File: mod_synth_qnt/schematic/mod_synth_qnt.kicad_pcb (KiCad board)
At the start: 2 copper layers, 41.3 x 109.2 mm, 37 parts, among them J1 CV IN, J2 Conn_02x08_Odd_Even, J3 QUANTIZE OUT, J4 Conn_01x07_Male, J5 Conn_01x07_Female, J6 Conn_01x07_Female, J7 Conn_01x07_Male, U1 LM358

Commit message: finish layout
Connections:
- A1 pad 5: /LED_A -> Net-(A1-Pad5)
- A1 pad 6: /LED_B -> Net-(A1-Pad6)
- A1 pad 7: /LED_C -> Net-(A1-Pad7)
- A1 pad 8: /LED_D -> Net-(A1-Pad8)
- C4 pad 1: /SCALE_SELECT -> /SCALE_SELECT_PCB_B
- C5 pad 1: /NOTE_SELECT -> /NOTE_SELECT_PCB_B
- D10 pad 1: Net-(D10-Pad1) -> /LED_B_PCB_B
- D10 pad 2: Net-(D10-Pad2) -> /LED_D_PCB_B
- D11 pad 1: Net-(D10-Pad2) -> /LED_D_PCB_B
- D11 pad 2: Net-(D10-Pad1) -> /LED_B_PCB_B
- D12 pad 1: Net-(D12-Pad1) -> /LED_A_PCB_B
- D12 pad 2: Net-(D10-Pad2) -> /LED_D_PCB_B
- D13 pad 1: Net-(D10-Pad2) -> /LED_D_PCB_B
- D13 pad 2: Net-(D12-Pad1) -> /LED_A_PCB_B
- D2 pad 1: Net-(D12-Pad1) -> /LED_A_PCB_B
- D2 pad 2: Net-(D10-Pad1) -> /LED_B_PCB_B
- D3 pad 1: Net-(D10-Pad1) -> /LED_B_PCB_B
- D3 pad 2: Net-(D3-Pad2) -> /LED_C_PCB_B
- D4 pad 1: Net-(D3-Pad2) -> /LED_C_PCB_B
- D4 pad 2: Net-(D10-Pad2) -> /LED_D_PCB_B
- D5 pad 1: Net-(D10-Pad1) -> /LED_B_PCB_B
- D5 pad 2: Net-(D12-Pad1) -> /LED_A_PCB_B
- D6 pad 1: Net-(D3-Pad2) -> /LED_C_PCB_B
- D6 pad 2: Net-(D10-Pad1) -> /LED_B_PCB_B
- D7 pad 1: Net-(D10-Pad2) -> /LED_D_PCB_B
- D7 pad 2: Net-(D3-Pad2) -> /LED_C_PCB_B
- D8 pad 1: Net-(D12-Pad1) -> /LED_A_PCB_B
- D8 pad 2: Net-(D3-Pad2) -> /LED_C_PCB_B
- D9 pad 1: Net-(D3-Pad2) -> /LED_C_PCB_B
- D9 pad 2: Net-(D12-Pad1) -> /LED_A_PCB_B
- J4 pad 5: Net-(J4-Pad5) -> /5V_PCB_B
- J5 pad 5: Net-(J5-Pad5) -> +5V
- J6 pad 2: Net-(J6-Pad2) -> /LED_A
- J6 pad 3: Net-(J6-Pad3) -> /LED_B
- J6 pad 4: Net-(J6-Pad4) -> /LED_C
- J6 pad 5: Net-(J6-Pad5) -> /LED_D
- J6 pad 6: Net-(J6-Pad6) -> /SCALE_SELECT
- J6 pad 7: Net-(J6-Pad7) -> /NOTE_SELECT
- J7 pad 2: Net-(J7-Pad2) -> /LED_A_PCB_B
- J7 pad 3: Net-(J7-Pad3) -> /LED_B_PCB_B
- J7 pad 4: Net-(J7-Pad4) -> /LED_C_PCB_B
- J7 pad 5: Net-(J7-Pad5) -> /LED_D_PCB_B
- J7 pad 6: Net-(J7-Pad6) -> /SCALE_SELECT_PCB_B
- J7 pad 7: Net-(J7-Pad7) -> /NOTE_SELECT_PCB_B
- R3 pad 1: Net-(D12-Pad1) -> /LED_A
- R3 pad 2: /LED_A -> Net-(A1-Pad5)
- R4 pad 1: Net-(D10-Pad1) -> /LED_B
- R4 pad 2: /LED_B -> Net-(A1-Pad6)
- R5 pad 1: Net-(D3-Pad2) -> /LED_C
- R5 pad 2: /LED_C -> Net-(A1-Pad7)
- R6 pad 1: Net-(D10-Pad2) -> /LED_D
- R6 pad 2: /LED_D -> Net-(A1-Pad8)
- RV1 pad 1: +5V -> /5V_PCB_B
- RV1 pad 2: /NOTE_SELECT -> /NOTE_SELECT_PCB_B
- RV2 pad 1: +5V -> /5V_PCB_B
- RV2 pad 2: /SCALE_SELECT -> /SCALE_SELECT_PCB_B
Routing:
- net /LED_A_PCB_B: track 0.00 -> 108.2 mm
- net /LED_D_PCB_B: track 0.00 -> 103.0 mm
- net /LED_C_PCB_B: track 0.00 -> 101.4 mm
- net /5V_PCB_B: track 0.00 -> 97.1 mm
- net /LED_B_PCB_B: track 0.00 -> 96.3 mm
- net Net-(D3-Pad2): track 57.6 -> 0.00 mm
- net +5V: track 29.3 -> 86.1 mm
- net Net-(D12-Pad1): track 56.0 -> 0.00 mm
- net Net-(D10-Pad1): track 55.4 -> 0.00 mm
- net Net-(D10-Pad2): track 53.1 -> 0.00 mm
- net /LED_A: track 17.5 -> 59.4 mm
- net /LED_B: track 20.1 -> 59.1 mm
- net /SCALE_SELECT_PCB_B: track 0.00 -> 38.3 mm
- net /LED_C: track 24.0 -> 58.8 mm
- net /LED_D: track 27.8 -> 59.3 mm
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
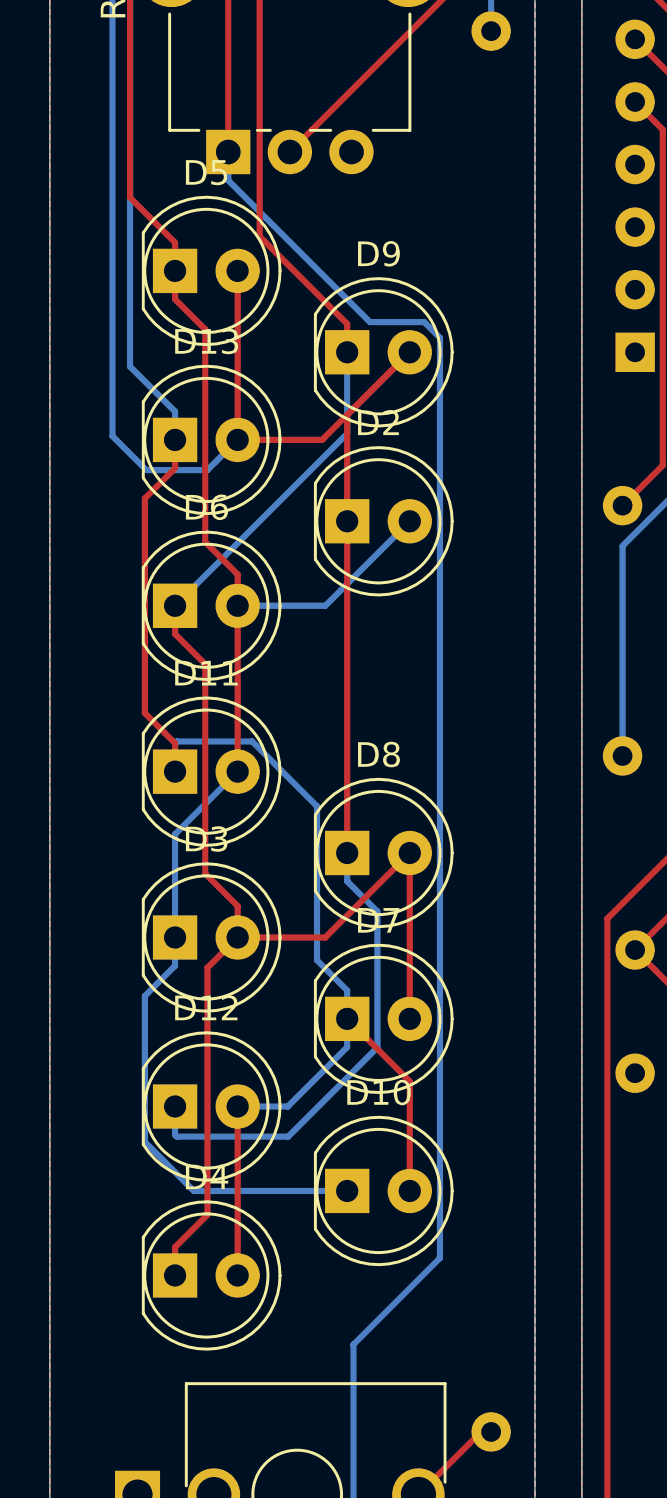
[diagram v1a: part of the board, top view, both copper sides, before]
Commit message: Use 3mm LEDs for panel hole clearance
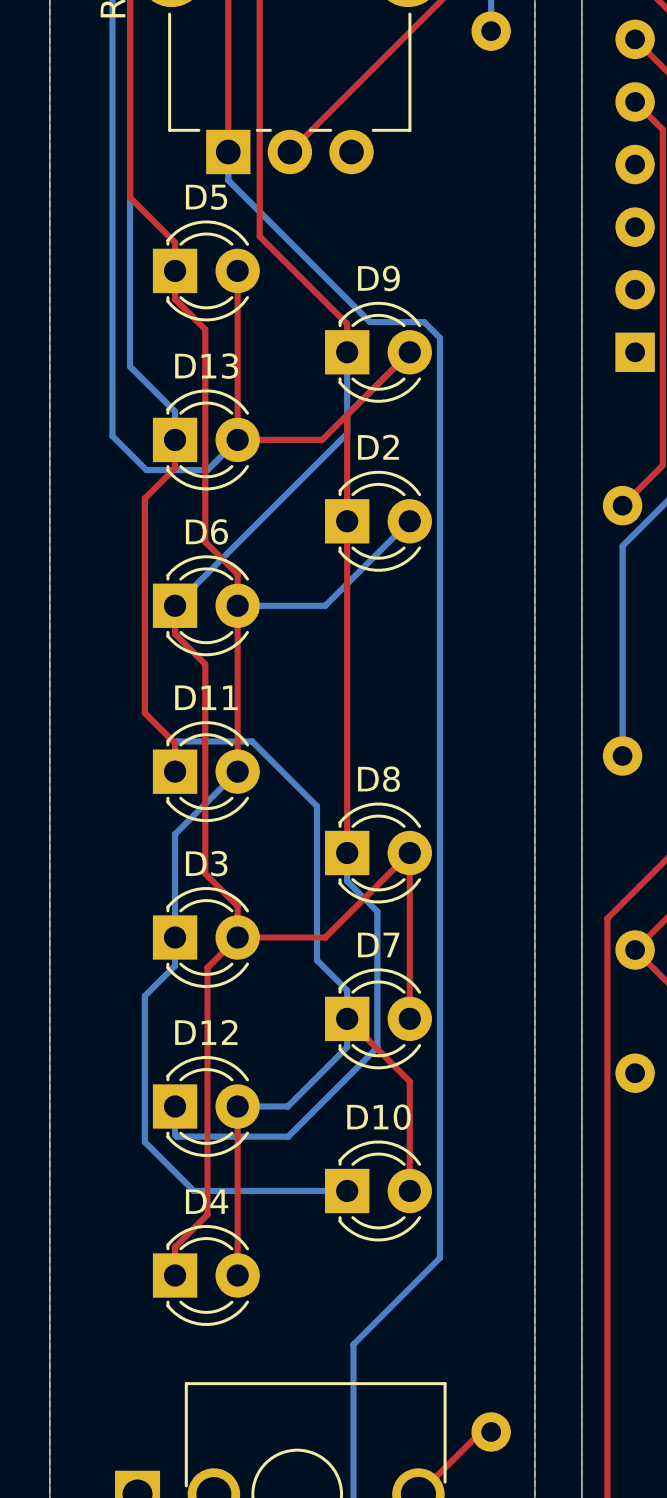
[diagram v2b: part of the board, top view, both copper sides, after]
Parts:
- D10, D11, D12, D13, D2, D3, D4, D5, D6, D7, D8, D9: footprint LED_THT:LED_D5.0mm -> LED_THT:LED_D3.0mm
